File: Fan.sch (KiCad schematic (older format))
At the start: 9 parts

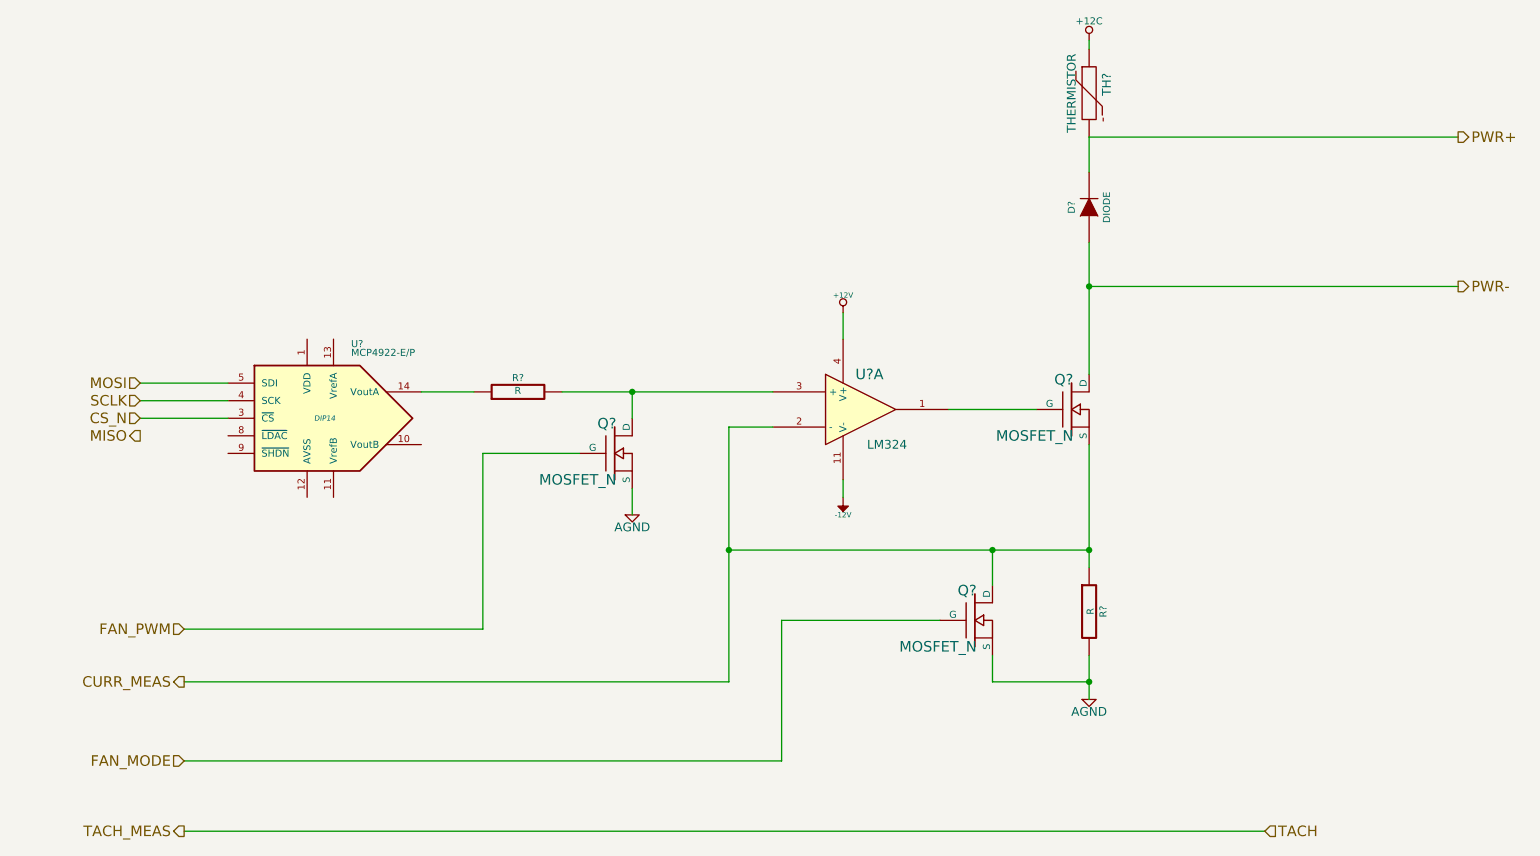
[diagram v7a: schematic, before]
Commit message: RELAY 02-20-2014
1) Created and associated footprints for relay module
2) Placed relay module's components in PCB layout
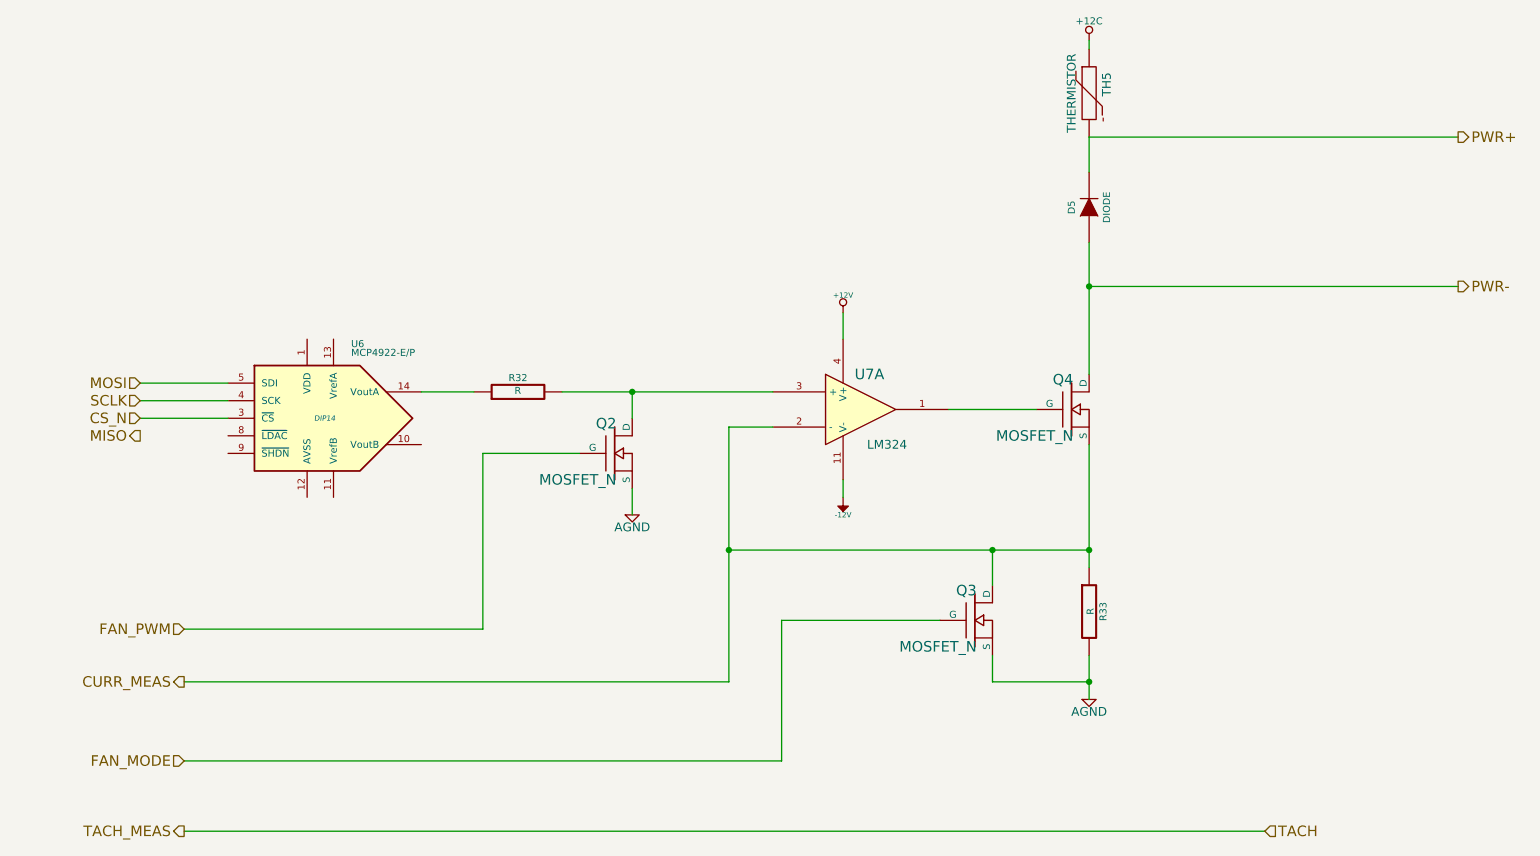
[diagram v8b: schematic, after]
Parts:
- gave numbers to parts that had none: 9
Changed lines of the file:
@@
 Sheet 6 9
 Title ""
-Date "11 feb 2014"
+Date "20 feb 2014"
 Rev ""
 Comp ""
@@
 TACH
 $Comp
-L LM324 U?
+L LM324 U7
 U 1 1 52F5F7EF
 P 6350 2750
-F 0 "U?" H 6400 2950 60  0000 C CNN
+F 0 "U7" H 6400 2950 60  0000 C CNN
 F 1 "LM324" H 6500 2550 50  0000 C CNN
 F 2 "~" H 6350 2750 60  0000 C CNN
@@
 $EndComp
 $Comp
-L MOSFET_N Q?
+L MOSFET_N Q4
 U 1 1 52F5F7FE
 P 7550 2750
-F 0 "Q?" H 7560 2920 60  0000 R CNN
+F 0 "Q4" H 7560 2920 60  0000 R CNN
 F 1 "MOSFET_N" H 7560 2600 60  0000 R CNN
 F 2 "~" H 7550 2750 60  0000 C CNN
@@
 	6850 2750 7350 2750
 Wire Wire Line
-	7650 2950 7650 3550
-Wire Wire Line
-	7650 3550 7650 3650
-$Comp
-L R R?
+	7650 2950 7650 3650
+$Comp
+L R R33
 U 1 1 52F5F820
 P 7650 3900
-F 0 "R?" V 7730 3900 40  0000 C CNN
+F 0 "R33" V 7730 3900 40  0000 C CNN
 F 1 "R" V 7657 3901 40  0000 C CNN
 F 2 "~" V 7580 3900 30  0000 C CNN
@@
 $EndComp
 $Comp
-L AGND #PWR?
+L AGND #PWR41
 U 1 1 52F5F833
 P 7650 4400
-F 0 "#PWR?" H 7650 4400 40  0001 C CNN
+F 0 "#PWR41" H 7650 4400 40  0001 C CNN
 F 1 "AGND" H 7650 4330 50  0000 C CNN
 F 2 "" H 7650 4400 60  0000 C CNN
@@
 $EndComp
 Wire Wire Line
-	7650 4150 7650 4300
-Wire Wire Line
-	7650 4300 7650 4400
+	7650 4150 7650 4400
 Wire Wire Line
 	5850 2850 5600 2850
 Wire Wire Line
-	5600 2850 5600 3550
-Wire Wire Line
-	5600 3550 5600 4300
-$Comp
-L -12V #PWR?
+	5600 2850 5600 4300
+$Comp
+L -12V #PWR39
 U 1 1 52F5F850
 P 6250 3250
-F 0 "#PWR?" H 6250 3380 20  0001 C CNN
+F 0 "#PWR39" H 6250 3380 20  0001 C CNN
 F 1 "-12V" H 6250 3350 30  0000 C CNN
 F 2 "" H 6250 3250 60  0000 C CNN
@@
 	6250 3150 6250 3250
 $Comp
-L +12V #PWR?
+L +12V #PWR38
 U 1 1 52F5F867
 P 6250 2200
-F 0 "#PWR?" H 6250 2150 20  0001 C CNN
+F 0 "#PWR38" H 6250 2150 20  0001 C CNN
 F 1 "+12V" H 6250 2300 30  0000 C CNN
 F 2 "" H 6250 2200 60  0000 C CNN
@@
 	6250 2200 6250 2350
 $Comp
-L AGND #PWR?
+L AGND #PWR37
 U 1 1 52F5F8F6
 P 5050 3350
-F 0 "#PWR?" H 5050 3350 40  0001 C CNN
+F 0 "#PWR37" H 5050 3350 40  0001 C CNN
 F 1 "AGND" H 5050 3280 50  0000 C CNN
 F 2 "" H 5050 3350 60  0000 C CNN
@@
 	5050 3200 5050 3350
 $Comp
-L MCP4922-E/P U?
+L MCP4922-E/P U6
 U 1 1 52F5F90F
 P 3300 2800
-F 0 "U?" H 3450 3200 40  0000 L BNN
+F 0 "U6" H 3450 3200 40  0000 L BNN
 F 1 "MCP4922-E/P" H 3450 3150 40  0000 L BNN
 F 2 "DIP14" H 3300 2800 30  0000 C CIN
@@
 	5600 4300 2500 4300
 $Comp
-L R R?
+L R R32
 U 1 1 52F5F997
 P 4400 2650
-F 0 "R?" V 4480 2650 40  0000 C CNN
+F 0 "R32" V 4480 2650 40  0000 C CNN
 F 1 "R" V 4407 2651 40  0000 C CNN
 F 2 "~" V 4330 2650 30  0000 C CNN
@@
 	2250 2800 2750 2800
 $Comp
-L MOSFET_N Q?
+L MOSFET_N Q3
 U 1 1 52F9D0E4
 P 7000 3950
-F 0 "Q?" H 7010 4120 60  0000 R CNN
+F 0 "Q3" H 7010 4120 60  0000 R CNN
 F 1 "MOSFET_N" H 7010 3800 60  0000 R CNN
 F 2 "~" H 7000 3950 60  0000 C CNN
@@
 $EndComp
 $Comp
-L THERMISTOR TH?
+L THERMISTOR TH5
 U 1 1 52F9D118
 P 7650 950
-F 0 "TH?" V 7750 1000 50  0000 C CNN
+F 0 "TH5" V 7750 1000 50  0000 C CNN
 F 1 "THERMISTOR" V 7550 950 50  0000 C CNN
 F 2 "~" H 7650 950 60  0000 C CNN
@@
 	9750 2050 7650 2050
 Wire Wire Line
-	7650 1800 7650 2050
-Wire Wire Line
-	7650 2050 7650 2550
-$Comp
-L DIODE D?
+	7650 1800 7650 2550
+$Comp
+L DIODE D5
 U 1 1 52F9D192
 P 7650 1600
-F 0 "D?" H 7650 1700 40  0000 C CNN
+F 0 "D5" H 7650 1700 40  0000 C CNN
 F 1 "DIODE" H 7650 1500 40  0000 C CNN
 F 2 "~" H 7650 1600 60  0000 C CNN
@@
 Connection ~ 7650 4300
 Wire Wire Line
-	4650 2650 5050 2650
-Wire Wire Line
-	5050 2650 5850 2650
-$Comp
-L MOSFET_N Q?
+	4650 2650 5850 2650
+$Comp
+L MOSFET_N Q2
 U 1 1 52F9D29A
 P 4950 3000
-F 0 "Q?" H 4960 3170 60  0000 R CNN
+F 0 "Q2" H 4960 3170 60  0000 R CNN
 F 1 "MOSFET_N" H 4960 2850 60  0000 R CNN
 F 2 "~" H 4950 3000 60  0000 C CNN
@@
 FAN_MODE
 Wire Wire Line
-	5600 3550 7100 3550
-Wire Wire Line
-	7100 3550 7650 3550
+	5600 3550 7650 3550
 Wire Wire Line
 	7100 3750 7100 3550
@@
 	5900 4750 2500 4750
 $Comp
-L +12C #PWR?
+L +12C #PWR40
 U 1 1 52F9D6B5
 P 7650 650
-F 0 "#PWR?" H 7650 620 30  0001 C CNN
+F 0 "#PWR40" H 7650 620 30  0001 C CNN
 F 1 "+12C" H 7650 760 40  0000 C CNN
 F 2 "" H 7650 650 60  0000 C CNN
